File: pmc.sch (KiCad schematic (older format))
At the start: 143 parts, among them M1 LM46001, M2 TPS61040, M3 STM32F405RG, M4 REF3033, M5 TPS73633, M6 SN65HVD233, M7 UCC27211A, M8 UCC27211A, M9 UCC27211A, P1 BOOT, P10 CONN4, P11 DEBUG, P2 PWM, P3 HALL, P4 SPI, P5 CAN, P6 CONN4, P7 CONN4, P8 CONN4, P9 CONN4, Q1 BC857C, Q2 IPT007N06N, Q3 IPT007N06N, Q4 IPT007N06N, Q5 IPT007N06N, Q6 IPT007N06N, Q7 IPT007N06N, U1 AD8539, U2 AD8539, U3 AD8417, U4 AD8417

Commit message: A new design with two 6-layer pcbs.
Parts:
- added P12, P16: F1, foot:PLS-5, symbol PLS_5
- added P13, P17: F2, foot:PLS-5, symbol PLS_5
- added P14, P18: A1, foot:PLS-5, symbol PLS_5
- added P15, P19: A2, foot:PLS-5, symbol PLS_5
- added R45, R46: 1K 1%, foot:SM-0603, symbol R
- added R47: NF, foot:SM-0603, symbol R
- C1: value 100nF 100v -> 2.2uF 100v; footprint foot:SM-0805 -> foot:SM-1210
- C57, C59, C61: footprint foot:SM-1206 -> foot:SM-1210
- P1, P2: footprint foot:PAD-4 -> foot:PLS-4
- P11, P3, P4: footprint foot:PAD-6 -> foot:PLS-6
- P5: footprint foot:PAD-2 -> foot:PLS-2
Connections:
- net +12V: now also P12.2, P16.2
- net +3.3V: now also R47.2
- net +3.3VREF: now also P14.1, P18.1, R47.1
- net +36V: now also P12.1, P16.1
- net AGND: now also R19.2, P12.3, P13.1, P14.2, P15.1, P16.3, P17.1, P18.2, P19.1; no longer D2.1
- net CURRENT_A: now also R46.1; no longer M3.16 (PA2/ADC_IN2)
- net CURRENT_B: now also R45.1; no longer M3.8 (PC0/ADC_IN10)
- net EXT_NTC: now also C39.2, P3.2, R34.1; no longer M3.14 (PA0/WKUP/ADC_IN0)
- net FET_AH: now also P16.5; no longer M3.41 (PA8/TIM1_CH1)
- net FET_AL: now also P16.4; no longer M3.34 (PB13/TIM1_CH1N)
- net FET_BH: now also P17.3; no longer M3.42 (PA9/TIM1_CH2)
- net FET_BL: now also P17.2; no longer M3.35 (PB14/TIM1_CH2N)
- net FET_CH: now also P17.5; no longer M3.43 (PA10/TIM1_CH3)
- net FET_CL: now also P17.4; no longer M3.36 (PB15/TIM1_CH3N)
- net LED: now also D2.2; no longer R19.1
- net PCB_NTC: now also P19.2; no longer M3.11 (PC3/ADC_IN13)
- net VOLTAGE_A: now also U1.1, U1.2 (_), P19.3; no longer M3.17 (PA3/ADC_IN3), U1.6 (_), U1.7
- net VOLTAGE_B: now also P19.4; no longer M3.10 (PC2/ADC_IN12)
- net VOLTAGE_C: now also P19.5; no longer M3.9 (PC1/ADC_IN11)
- net VOLTAGE_U: now also U1.6 (_), U1.7, P18.5; no longer M3.15 (PA1/ADC_IN1), U1.1, U1.2 (_)
- net at C35.1, R26.2, R30.2: now also U1.5 (+); no longer U1.3 (+)
- net at C36.1, R27.2, R31.2: now also U1.3 (+); no longer U1.5 (+)
- new net: M3.14 (PA0/WKUP/ADC_IN0), R41.1
- new net: D2.1, R19.1
- new net: P18.3, R46.2
- new net: P18.4, R45.2
- new net ADC_IN1: M3.15 (PA1/ADC_IN1), P14.5
- new net ADC_IN10: M3.8 (PC0/ADC_IN10), P15.4
- new net ADC_IN11: M3.9 (PC1/ADC_IN11), P15.5
- new net ADC_IN12: M3.10 (PC2/ADC_IN12), P15.2
- new net ADC_IN13: M3.11 (PC3/ADC_IN13), P15.3
- new net ADC_IN2: M3.16 (PA2/ADC_IN2), P14.4
- new net ADC_IN3: M3.17 (PA3/ADC_IN3), P14.3
- new net TIM1_CH1: M3.41 (PA8/TIM1_CH1), P12.5
- new net TIM1_CH1N: M3.34 (PB13/TIM1_CH1N), P12.4
- new net TIM1_CH2: M3.42 (PA9/TIM1_CH2), P13.3
- new net TIM1_CH2N: M3.35 (PB14/TIM1_CH2N), P13.2
- new net TIM1_CH3: M3.43 (PA10/TIM1_CH3), P13.5
- new net TIM1_CH3N: M3.36 (PB15/TIM1_CH3N), P13.4
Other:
- note added: "Hardrware specification:\n* PCB dimension 52mm x 45mm\n* Single supply from 5V to 40V\n* Motor current up to 50A\n* PWM frequency 20kHz to 80kHz"
- note removed: "Hardrware specification:\n* PCB dimension 47mm x 45mm\n* Single supply from 5V to 40V\n* Motor current up to 50A\n* PWM frequency 20kHz to 80kHz"
- moved on the sheet: C10, C11, C15, C16, C21, C22, C24, C27, C35, C36, C37, C38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

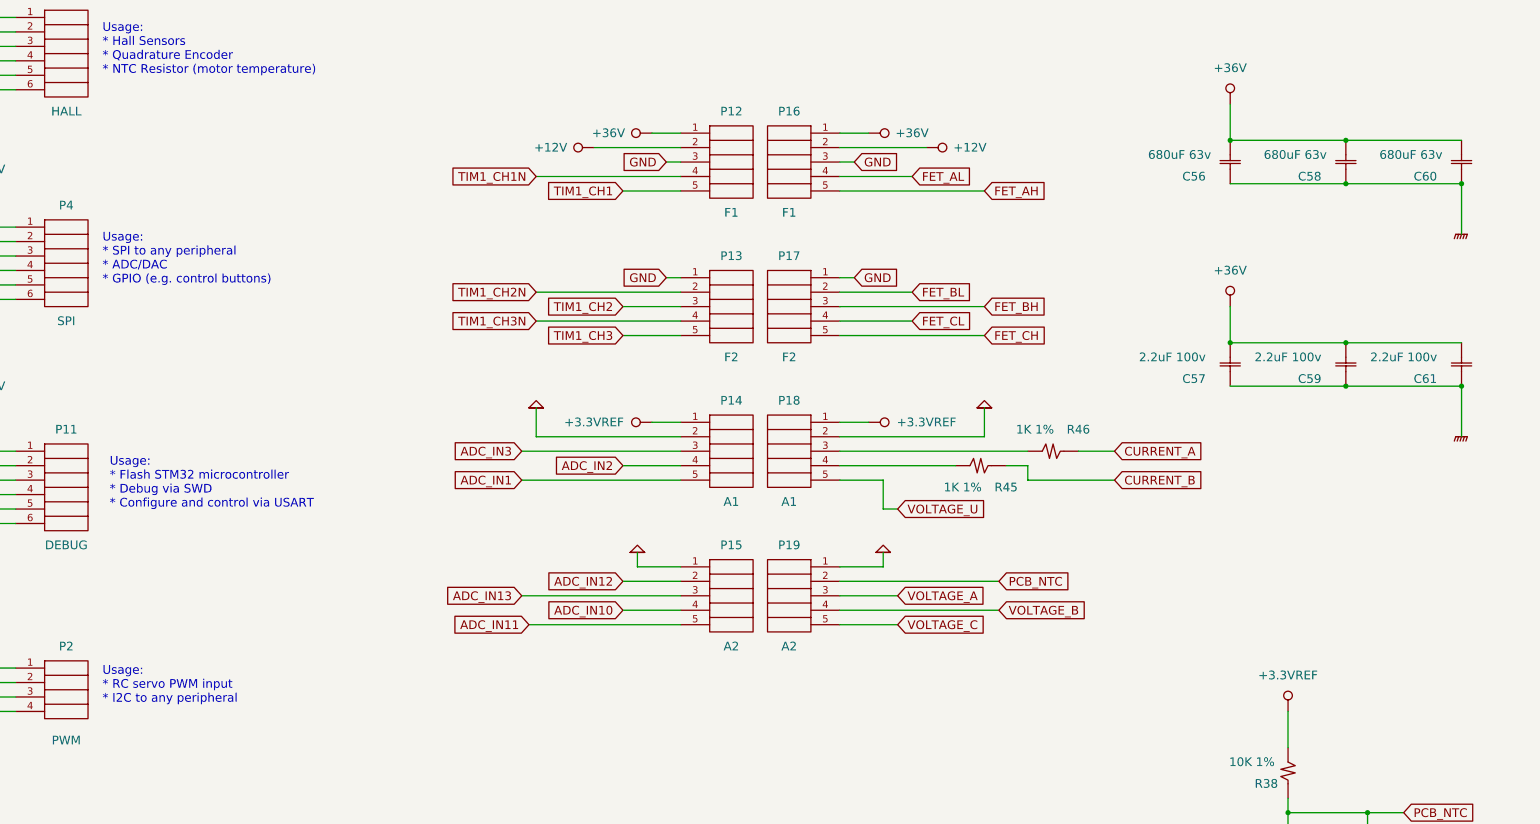
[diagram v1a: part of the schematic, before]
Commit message: Fixed routing of control pcb.
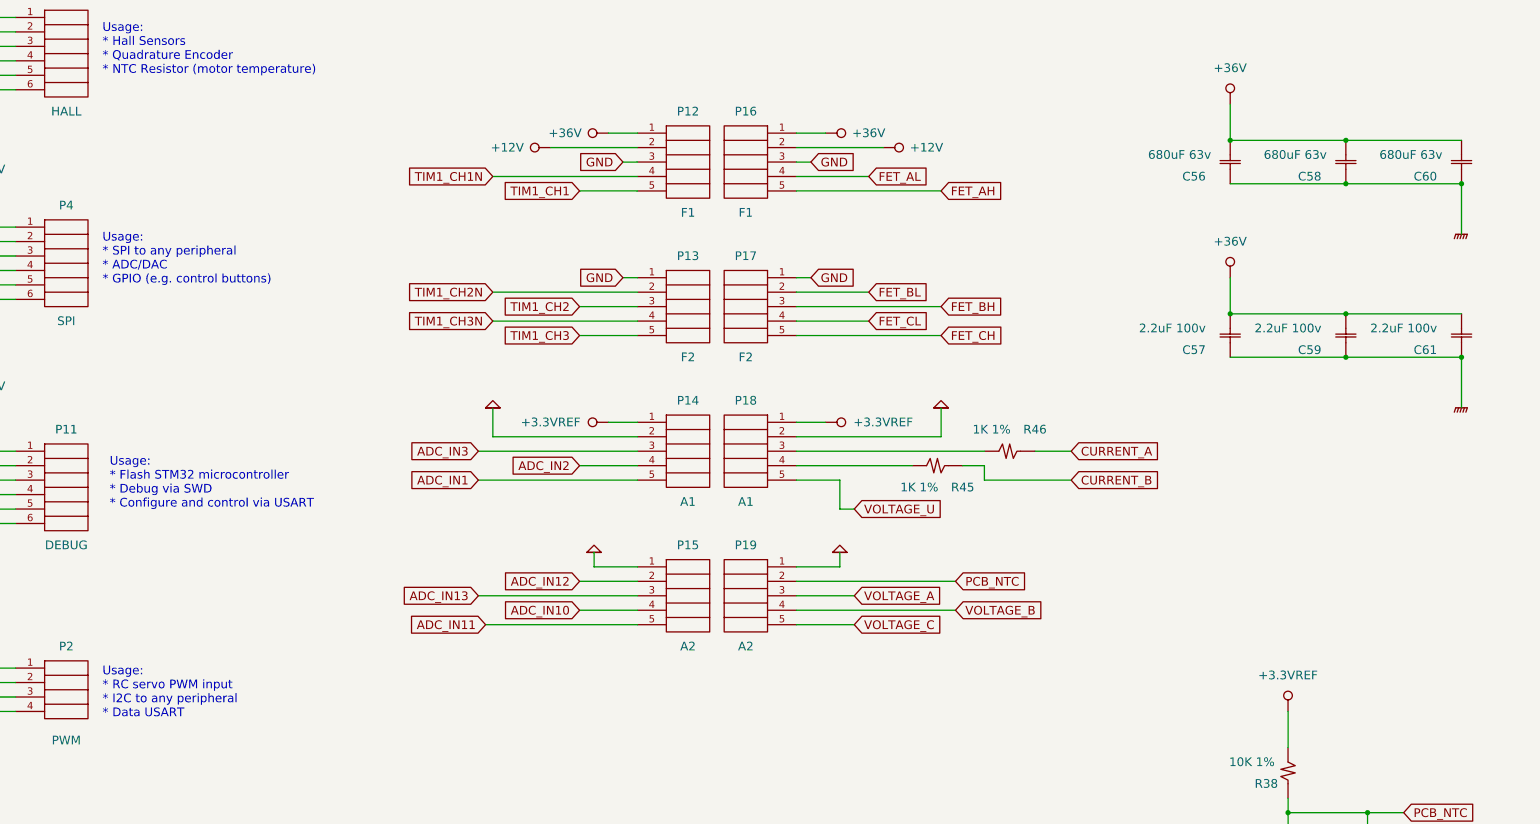
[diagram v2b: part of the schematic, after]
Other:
- note added: "Usage:\n* RC servo PWM input\n* I2C to any peripheral\n* Data USART"
- note removed: "Usage:\n* RC servo PWM input\n* I2C to any peripheral"
- moved on the sheet: C57, C59, C61, P12, P13, P14, P15, P16, P17, P18, P19, R45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

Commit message: Added analog input and FAN output.
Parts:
- removed P11: DEBUG, foot:PLS-6, symbol PLS_6
- removed P3: HALL, foot:PLS-6, symbol PLS_6
- removed Q1: BC857C, foot:SOT-23, symbol BJT-PNP
- removed R36, R37: 0.0005 1%, foot:LR2512-D, symbol R
- added C29: 10nF 25v, foot:SM-0603, symbol C
- added C62: 2.2uF 100v, foot:SM-1210, symbol C
- added P11: FAN, foot:PLS-2, symbol PLS_2
- added P20: ANALOG, foot:PLS-3, symbol PLS_3
- added P21: SWD, foot:PLS-4, symbol PLS_4
- added P22: USART, foot:PLS-4, symbol PLS_4
- added P23: HALL, foot:PLS-5, symbol PLS_5
- added P3: NTC, foot:PLS-2, symbol PLS_2
- added Q1: IRLML6401, foot:SOT-23, symbol P-MOSFET
- added R36, R37: 0.0003 1%, foot:LR2512-4, symbol R-4
- added R48: 1K, foot:SM-0603, symbol R
- added R49, R50: 10K 1%, foot:SM-0603, symbol R
- P2: value PWM -> PPM
- R10: value 27K 1% -> 25.5K 1%
- R12: value 11K 1% -> 11.3K 1%
- R41: value 1K -> 10K
- R47: value NF -> *NF
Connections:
- net +12V: now also C18.1, D1.1
- net +3.3V: now also P21.1, P22.1
- net +36V: now also C62.2
- net +5V: now also P20.1, P23.1, Q1.2 (S)
- net AGND: now also C29.1, C62.1, P11.2, P20.3, P21.4, P22.4, P23.5, P3.2, R49.1
- net EXT_NTC: now also P3.1; no longer C39.2
- net HALL_A: now also P23.2
- net HALL_B: now also P23.3
- net HALL_C: now also P23.4
- net SWCLK: now also P21.3
- net SWDIO: now also P21.2
- net TERMINAL_A: now also R36.2; no longer U3.1 (_)
- net TERMINAL_B: now also R37.2; no longer U4.1 (_)
- net USART_RX: now also P22.3
- net USART_TX: now also P22.2
- net at M3.14 (PA0/WKUP/ADC_IN0), R41.1: now also C39.2
- net ADC_IN14: now reaches M3.24 (PC4/ADC_IN14)
- net ADC_IN14: now also C29.2, R49.2, R50.1
- net FAN: now reaches M3.33 (PB12)
- net FAN: now also R48.1
- net at R8.2: now also Q1.1 (G), R48.2
- net at C52.1, C53.1, M8.4 (HS)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: now also R37.1; no longer U4.8 (+)
- net at C50.1, C51.1, M7.4 (HS)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: now also R36.1; no longer U3.8 (+)
- new net: R36.4, U3.1 (_)
- new net: R36.3, U3.8 (+)
- new net: R37.4, U4.1 (_)
- new net: R37.3, U4.8 (+)
- new net: P20.2, R50.2
- new net: P11.1, Q1.3 (D)
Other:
- note added: "(1) Balance resistors are needed only in case of parallel\nconnection of power boards\n\n(2) You have an option not to use voltage reference"
- note added: "(3) Current sensing range\n\nRange (A) Shunt (uOhm)\n-----------------\n 25 1000\n 50 500\n 80 300\n 100 250\n 130 187\n 160 150"
- note added: "- Analog input\n- Output 5v"
- note added: "- External FAN control (5v ~~0.3A)"
- note added: "- External NTC (motor temperature)"
- note added: "- Flash STM32 microcontroller\n- Debug via SWD\n- Configure and control via USART\n"
- note added: "- Hall Sensors\n- Quadrature Encoder\n- GPIO"
- note added: "- RC servo PPM input\n- STEP/DIR\n- Quadrature Encoder\n- I2C to any peripheral\n- Data USART"
- note added: "- SPI to any peripheral\n- ADC/DAC\n- GPIO"
- note added: "Designed hardrware specification:\n* PCBs dimension 52mm x 45mm\n* Single supply from 6V to 50V\n* Phase current up to 80A\n* PWM frequency 20kHz to 80kHz"
- note added: "Note (1)"
- note added: "Note (2)"
- note added: "Note (3)"
- note removed: "Hardrware specification:\n* PCB dimension 52mm x 45mm\n* Single supply from 5V to 40V\n* Motor current up to 50A\n* PWM frequency 20kHz to 80kHz"
- note removed: "Usage: CAN bus only"
- note removed: "Usage:\n* Flash STM32 microcontroller\n* Debug via SWD\n* Configure and control via USART\n"
- note removed: "Usage:\n* Hall Sensors\n* Quadrature Encoder\n* NTC Resistor (motor temperature)"
- note removed: "Usage:\n* RC servo PWM input\n* I2C to any peripheral\n* Data USART"
- note removed: "Usage:\n* SPI to any peripheral\n* ADC/DAC\n* GPIO (e.g. control buttons)"
- moved on the sheet: C1, C10, C11, C13, C14, C15, C16, C19, C20, C21, C22, C24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

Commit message: Improved step-up layout.
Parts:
- added D3: NSR0320, foot:SM-0805, symbol DIODE
- C35, C36, C37, C38: value 120pF -> 47pF C0G
- D1: footprint foot:SOD-232 -> foot:SM-0805
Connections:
- net AGND: now also D3.2
- net at P11.1, Q1.3 (D): now also D3.1
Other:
- moved on the sheet: P11, P3
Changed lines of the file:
@@
 Sheet 1 1
 Title "Phobia Motor Controller"
-Date "2018-10-21"
+Date "2018-11-09"
 Rev "4c"
 Comp "Roman Belov"
@@
 F 0 "D1" H 4100 4500 60  0000 C CNN
 F 1 "NSR0320" H 4250 4750 60  0000 C CNN
-F 2 "foot:SOD-232" H 4200 4600 60  0001 C CNN
+F 2 "foot:SM-0805" H 4200 4600 60  0001 C CNN
 F 3 "" H 4200 4600 60  0000 C CNN
 	1    4200 4600
@@
 U 1 1 59D9347A
 P 2800 11600
-F 0 "D2" H 2700 11450 60  0000 C CNN
-F 1 "LED" H 3000 11450 60  0000 C CNN
+F 0 "D2" H 2750 11450 60  0000 C CNN
+F 1 "LED" H 2950 11450 60  0000 C CNN
 F 2 "foot:SM-0603" H 2800 11600 60  0001 C CNN
 F 3 "" H 2800 11600 60  0000 C CNN
@@
 P 13250 2050
 F 0 "C35" V 13350 1850 60  0000 C CNN
-F 1 "120pF" V 13200 1800 60  0000 C CNN
+F 1 "47pF C0G" V 13150 1700 60  0000 C CNN
 F 2 "foot:SM-0603" H 13250 2050 60  0001 C CNN
 F 3 "" H 13250 2050 60  0000 C CNN
@@
 P 13250 3400
 F 0 "C36" V 13350 3200 60  0000 C CNN
-F 1 "120pF" V 13200 3150 60  0000 C CNN
+F 1 "47pF C0G" V 13150 3050 60  0000 C CNN
 F 2 "foot:SM-0603" H 13250 3400 60  0001 C CNN
 F 3 "" H 13250 3400 60  0000 C CNN
@@
 P 13250 4750
 F 0 "C37" V 13350 4550 60  0000 C CNN
-F 1 "120pF" V 13200 4500 60  0000 C CNN
+F 1 "47pF C0G" V 13150 4400 60  0000 C CNN
 F 2 "foot:SM-0603" H 13250 4750 60  0001 C CNN
 F 3 "" H 13250 4750 60  0000 C CNN
@@
 P 13250 6100
 F 0 "C38" V 13350 5900 60  0000 C CNN
-F 1 "120pF" V 13200 5850 60  0000 C CNN
+F 1 "47pF C0G" V 13150 5750 60  0000 C CNN
 F 2 "foot:SM-0603" H 13250 6100 60  0001 C CNN
 F 3 "" H 13250 6100 60  0000 C CNN
@@
 	1    0    0    -1
 $EndComp
-Text GLabel 8350 6100 0    60   Input ~ 0
+Text GLabel 8550 6100 0    60   Input ~ 0
 EXT_NTC
 $Comp
@@
 Text Notes 15100 14100 0    60   ~ 0
 - Flash STM32 microcontroller\n- Debug via SWD\n- Configure and control via USART\n
-Text Notes 20800 14400 0    60   ~ 12
+Text Notes 20950 14000 0    60   ~ 12
 Designed hardrware specification:\n* PCBs dimension 52mm x 45mm\n* Single supply from 6V to 50V\n* Phase current up to 80A\n* PWM frequency 20kHz to 80kHz
 $Comp
@@
 L PLS_2 P11
 U 1 1 5BD9943A
-P 9150 4750
-F 0 "P11" H 9150 4950 60  0000 C CNN
-F 1 "FAN" H 9150 4550 60  0000 C CNN
-F 2 "foot:PLS-2" H 8800 4500 60  0001 C CNN
-F 3 "" H 9300 4350 60  0000 C CNN
-	1    9150 4750
+P 9350 4750
+F 0 "P11" H 9350 4950 60  0000 C CNN
+F 1 "FAN" H 9350 4550 60  0000 C CNN
+F 2 "foot:PLS-2" H 9000 4500 60  0001 C CNN
+F 3 "" H 9500 4350 60  0000 C CNN
+	1    9350 4750
 	1    0    0    -1
 $EndComp
@@
 FAN
 $Comp
-L GND #PWR0100
-U 1 1 5BDB0346
-P 8750 5000
-F 0 "#PWR0100" H 8750 5000 30  0001 C CNN
-F 1 "GND" H 8750 4930 30  0001 C CNN
-F 2 "" H 8750 5000 60  0000 C CNN
-F 3 "" H 8750 5000 60  0000 C CNN
-	1    8750 5000
-	1    0    0    -1
-$EndComp
-$Comp
 L R-4 R36
 U 1 1 5BCE1EB0
@@
 $EndComp
 $Comp
-L +5V #PWR0101
+L +5V #PWR0100
 U 1 1 5BD3BAA5
 P 11800 11200
-F 0 "#PWR0101" H 11800 11290 20  0001 C CNN
+F 0 "#PWR0100" H 11800 11290 20  0001 C CNN
 F 1 "+5V" H 11800 11450 60  0000 C CNN
 F 2 "" H 11800 11200 60  0000 C CNN
@@
 $EndComp
 $Comp
-L GND #PWR0102
+L GND #PWR0101
 U 1 1 5BD3C43D
 P 11800 12300
-F 0 "#PWR0102" H 11800 12300 30  0001 C CNN
+F 0 "#PWR0101" H 11800 12300 30  0001 C CNN
 F 1 "GND" H 11800 12230 30  0001 C CNN
 F 2 "" H 11800 12300 60  0000 C CNN
@@
 	3550 1900 3550 2100
 Wire Wire Line
-	6350 2900 6350 1900
+	6350 1900 6350 2900
 Wire Wire Line
 	3900 4600 4050 4600
@@
 Connection ~ 2750 8550
 Wire Wire Line
-	8800 4700 8550 4700
-Wire Wire Line
 	7600 4700 8050 4700
 Wire Wire Line
@@
 	7950 5400 7550 5400
 Wire Wire Line
-	8800 4800 8750 4800
-Wire Wire Line
-	8750 4800 8750 5000
-Wire Wire Line
 	20700 2350 20550 2350
 Wire Wire Line
@@
 $EndComp
 $Comp
-L GND #PWR0103
+L GND #PWR0102
 U 1 1 5BD0556F
 P 7100 11600
-F 0 "#PWR0103" H 7100 11600 30  0001 C CNN
+F 0 "#PWR0102" H 7100 11600 30  0001 C CNN
 F 1 "GND" H 7100 11530 30  0001 C CNN
 F 2 "" H 7100 11600 60  0000 C CNN
@@
 SWDIO
 $Comp
-L GND #PWR0104
+L GND #PWR0103
 U 1 1 5BD0CAEE
 P 14400 15300
-F 0 "#PWR0104" H 14400 15300 30  0001 C CNN
+F 0 "#PWR0103" H 14400 15300 30  0001 C CNN
 F 1 "GND" H 14400 15230 30  0001 C CNN
 F 2 "" H 14400 15300 60  0000 C CNN
@@
 $EndComp
 $Comp
-L +3.3V #PWR0105
+L +3.3V #PWR0104
 U 1 1 5BD0CCE5
 P 14300 13600
-F 0 "#PWR0105" H 14300 13690 20  0001 C CNN
+F 0 "#PWR0104" H 14300 13690 20  0001 C CNN
 F 1 "+3.3V" H 14300 13850 60  0000 C CNN
 F 2 "" H 14300 13600 60  0000 C CNN
@@
 L PLS_2 P3
 U 1 1 5BD414B8
-P 9150 6150
-F 0 "P3" H 9150 6350 60  0000 C CNN
-F 1 "NTC" H 9150 5950 60  0000 C CNN
-F 2 "foot:PLS-2" H 8800 5900 60  0001 C CNN
-F 3 "" H 9300 5750 60  0000 C CNN
-	1    9150 6150
+P 9350 6150
+F 0 "P3" H 9350 6350 60  0000 C CNN
+F 1 "NTC" H 9350 5950 60  0000 C CNN
+F 2 "foot:PLS-2" H 9000 5900 60  0001 C CNN
+F 3 "" H 9500 5750 60  0000 C CNN
+	1    9350 6150
 	1    0    0    -1
 $EndComp
 Wire Wire Line
-	8600 6400 8600 6200
+	8800 6400 8800 6200
 Wire Wire Line
-	8600 6200 8800 6200
+	8800 6200 9000 6200
 Wire Wire Line
-	8800 6100 8350 6100
+	9000 6100 8550 6100
 Wire Wire Line
 	11200 7500 12000 7500
@@
 Wire Wire Line
 	11200 7700 12000 7700
-Text Notes 9400 6150 0    60   ~ 0
+Text Notes 9600 6150 0    60   ~ 0
 - External NTC (motor temperature)
 $Comp
-L AGND #PWR0106
+L AGND #PWR0105
 U 1 1 5BD4E297
-P 8600 6400
-F 0 "#PWR0106" H 8600 6400 30  0001 C CNN
-F 1 "AGND" H 8600 6330 30  0001 C CNN
-F 2 "~" H 8600 6400 60  0000 C CNN
-F 3 "~" H 8600 6400 60  0000 C CNN
-	1    8600 6400
+P 8800 6400
+F 0 "#PWR0105" H 8800 6400 30  0001 C CNN
+F 1 "AGND" H 8800 6330 30  0001 C CNN
+F 2 "~" H 8800 6400 60  0000 C CNN
+F 3 "~" H 8800 6400 60  0000 C CNN
+	1    8800 6400
 	1    0    0    -1
 $EndComp
-Text Notes 9400 4750 0    60   ~ 0
+Text Notes 9600 4750 0    60   ~ 0
 - External FAN control (5v ~~0.3A)
-Text Notes 18450 13250 0    60   ~ 12
+Text Notes 18050 13250 0    60   ~ 12
 (3) Current sensing range\n\nRange (A)   Shunt (uOhm)\n-----------------\n      25       1000\n      50       500\n      80       300\n     100       250\n     130       187\n     160       150
 Text Notes 20250 1950 0    60   ~ 12
@@
 Wire Wire Line
 	7700 10600 8100 10600
+$Comp
+L DIODE D3
+U 1 1 5BE5E5EA
+P 8950 5400
+F 0 "D3" H 8800 5300 60  0000 C CNN
+F 1 "NSR0320" H 9050 5600 60  0000 C CNN
+F 2 "foot:SM-0805" H 8950 5400 60  0001 C CNN
+F 3 "" H 8950 5400 60  0000 C CNN
+	1    8950 5400
+	-1   0    0    1
+$EndComp
+$Comp
+L GND #PWR0106
+U 1 1 5BE605BE
+P 9350 5550
+F 0 "#PWR0106" H 9350 5550 30  0001 C CNN
+F 1 "GND" H 9350 5480 30  0001 C CNN
+F 2 "" H 9350 5550 60  0000 C CNN
+F 3 "" H 9350 5550 60  0000 C CNN
+	1    9350 5550
+	1    0    0    -1
+$EndComp
+Wire Wire Line
+	9350 5100 9350 5550
+Wire Wire Line
+	9350 5100 8900 5100
+Wire Wire Line
+	8900 5100 8900 4800
+Wire Wire Line
+	8900 4800 9000 4800
+Wire Wire Line
+	9100 5400 9350 5400
+Connection ~ 9350 5400
+Wire Wire Line
+	8550 4700 9000 4700
+Wire Wire Line
+	8750 5400 8650 5400
+Wire Wire Line
+	8650 5400 8650 4700
+Connection ~ 8650 4700
 $EndSCHEMATC

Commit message: New annotation.
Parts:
- renumbered C62 to C1, C16 to C10, C3 to C11, C7 to C12, C39 to C13, C8 to C14, C9 to C15, C21 to C16, C22 to C17, C12 to C18, C24 to C19, C17 to C20, C40 to C21, C18 to C22, C27 to C23, C13 to C24, C14 to C25, C43 to C26, C19 to C27, C23 to C28, C20 to C29, C10 to C3, C25 to C30, C26 to C31, C28 to C32, C30 to C33, C31 to C34, C41 to C35, C42 to C36, C32 to C37, C33 to C38, C34 to C39, C11 to C4, C29 to C40, C35 to C41, C36 to C42, C37 to C43, C38 to C44, C44 to C45, C45 to C46, C46 to C47, C47 to C48, C48 to C49, C1 to C5, C49 to C50, C50 to C51, C51 to C52, C52 to C53, C53 to C54, C54 to C55, C55 to C56, C56 to C57, C57 to C58, C58 to C59, C4 to C6, C59 to C60, C64 to C61, C65 to C62, C66 to C63, C60 to C64, C61 to C65, C5 to C7, C6 to C8, C15 to C9, D2 to D1, D1 to D2, M2 to M1, M1 to M2, P11 to P1, P12 to P10, P13 to P11, P14 to P12, P15 to P13, P1 to P14, P16 to P15, P17 to P16, P18 to P17, P19 to P18, P6 to P19, P3 to P2, P7 to P20, P8 to P21, P9 to P22, P10 to P23, P23 to P3, P2 to P5, P20 to P6, P5 to P7, P21 to P8, P22 to P9, R34 to R1, R13 to R11, R14 to R12, R15 to R13, R40 to R14, R16 to R15, R17 to R16, R18 to R17, R42 to R18, R8 to R19, R19 to R2, R1 to R20, R3 to R21, R48 to R22, R20 to R23, R21 to R24, R22 to R25, R2 to R26, R4 to R27, R23 to R28, R24 to R29, R41 to R3, R25 to R30, R43 to R31, R44 to R32, R47 to R33, R49 to R34, R50 to R36, R26 to R37, R27 to R38, R28 to R39, R6 to R4, R29 to R40, R30 to R41, R31 to R42, R32 to R43, R33 to R44, R36 to R47, R37 to R48, R38 to R49, R39 to R50, R7 to R6, R11 to R7, R12 to R8

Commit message: Updated to rev4c.
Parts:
- added R51: 820, foot:SM-1206, symbol R
- D3: value NSR0320 -> 1N4448WS
- R33: value *NF -> 1
- R35: value 120 -> 820
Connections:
- net AGND: now also D1.1; no longer R2.2
- net LED: now also R2.1; no longer D1.2
- net at M6.6 (CANL), P7.2, R35.1: now also R51.1
- net at M6.7 (CANH), P7.1, R35.2: now also R51.2
- new net: D1.2, R2.2
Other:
- note added: "Analog control input\n5v supply ouput"
- note added: "Balance resistors R45-R46 are needed only in case of parallel\nconnection of multiple power boards\n"
- note added: "CAN bus"
- note added: "Current sensing range\n\nRange (A) Shunt (mOhm)\n-----------------\n 50 0.5\n 80 0.3\n 100 0.25"
- note added: "External FAN control (5v ~~0.3A)"
- note added: "External NTC (10K)"
- note added: "External peripheral SPI device\nor ADC/DAC or GPIO"
- note added: "Flash STM32 microcontroller\nDebug via SWD\nConfigure and control via USART\n"
- note added: "Motor interface:\n * Hall Sensors\n * Quadrature Encoder\nor GPIO"
- note added: "Optional termination resistors"
- note added: "Pulse control inputs:\n * RC servo PPM\n * STEP/DIR\n * QEP\nor I2C bus or USART"
- note added: "R33 is not fitted if 3.3vREF voltage reference is used\n"
- note removed: "(1) Balance resistors are needed only in case of parallel\nconnection of power boards\n\n(2) You have an option not to use voltage reference"
- note removed: "(3) Current sensing range\n\nRange (A) Shunt (uOhm)\n-----------------\n 25 1000\n 50 500\n 80 300\n 100 250\n 130 187\n 160 150"
- note removed: "- Analog input\n- Output 5v"
- note removed: "- External FAN control (5v ~~0.3A)"
- note removed: "- External NTC (motor temperature)"
- note removed: "- Flash STM32 microcontroller\n- Debug via SWD\n- Configure and control via USART\n"
- note removed: "- Hall Sensors\n- Quadrature Encoder\n- GPIO"
- note removed: "- RC servo PPM input\n- STEP/DIR\n- Quadrature Encoder\n- I2C to any peripheral\n- Data USART"
- note removed: "- SPI to any peripheral\n- ADC/DAC\n- GPIO"
- note removed: "Note (1)"
- note removed: "Note (2)"
- note removed: "Note (3)"
- moved on the sheet: C57, C58, C59, C60, C64, C65, D1, R2, R35
